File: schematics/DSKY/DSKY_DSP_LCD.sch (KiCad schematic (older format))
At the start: 12 parts

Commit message: Minor DSKY tweaks.
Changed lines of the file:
@@
 $Descr A 8500 11000 portrait
 encoding utf-8
-Sheet 12 15
+Sheet 11 15
 Title ""
 Date ""
@@
 	1450 8250 1250 8250
 Wire Bus Line
-	700  2550 7000 2550
-Wire Bus Line
 	700  4500 7200 4500
 Wire Bus Line
+	700  2550 7200 2550
+Wire Bus Line
 	700  6500 7200 6500

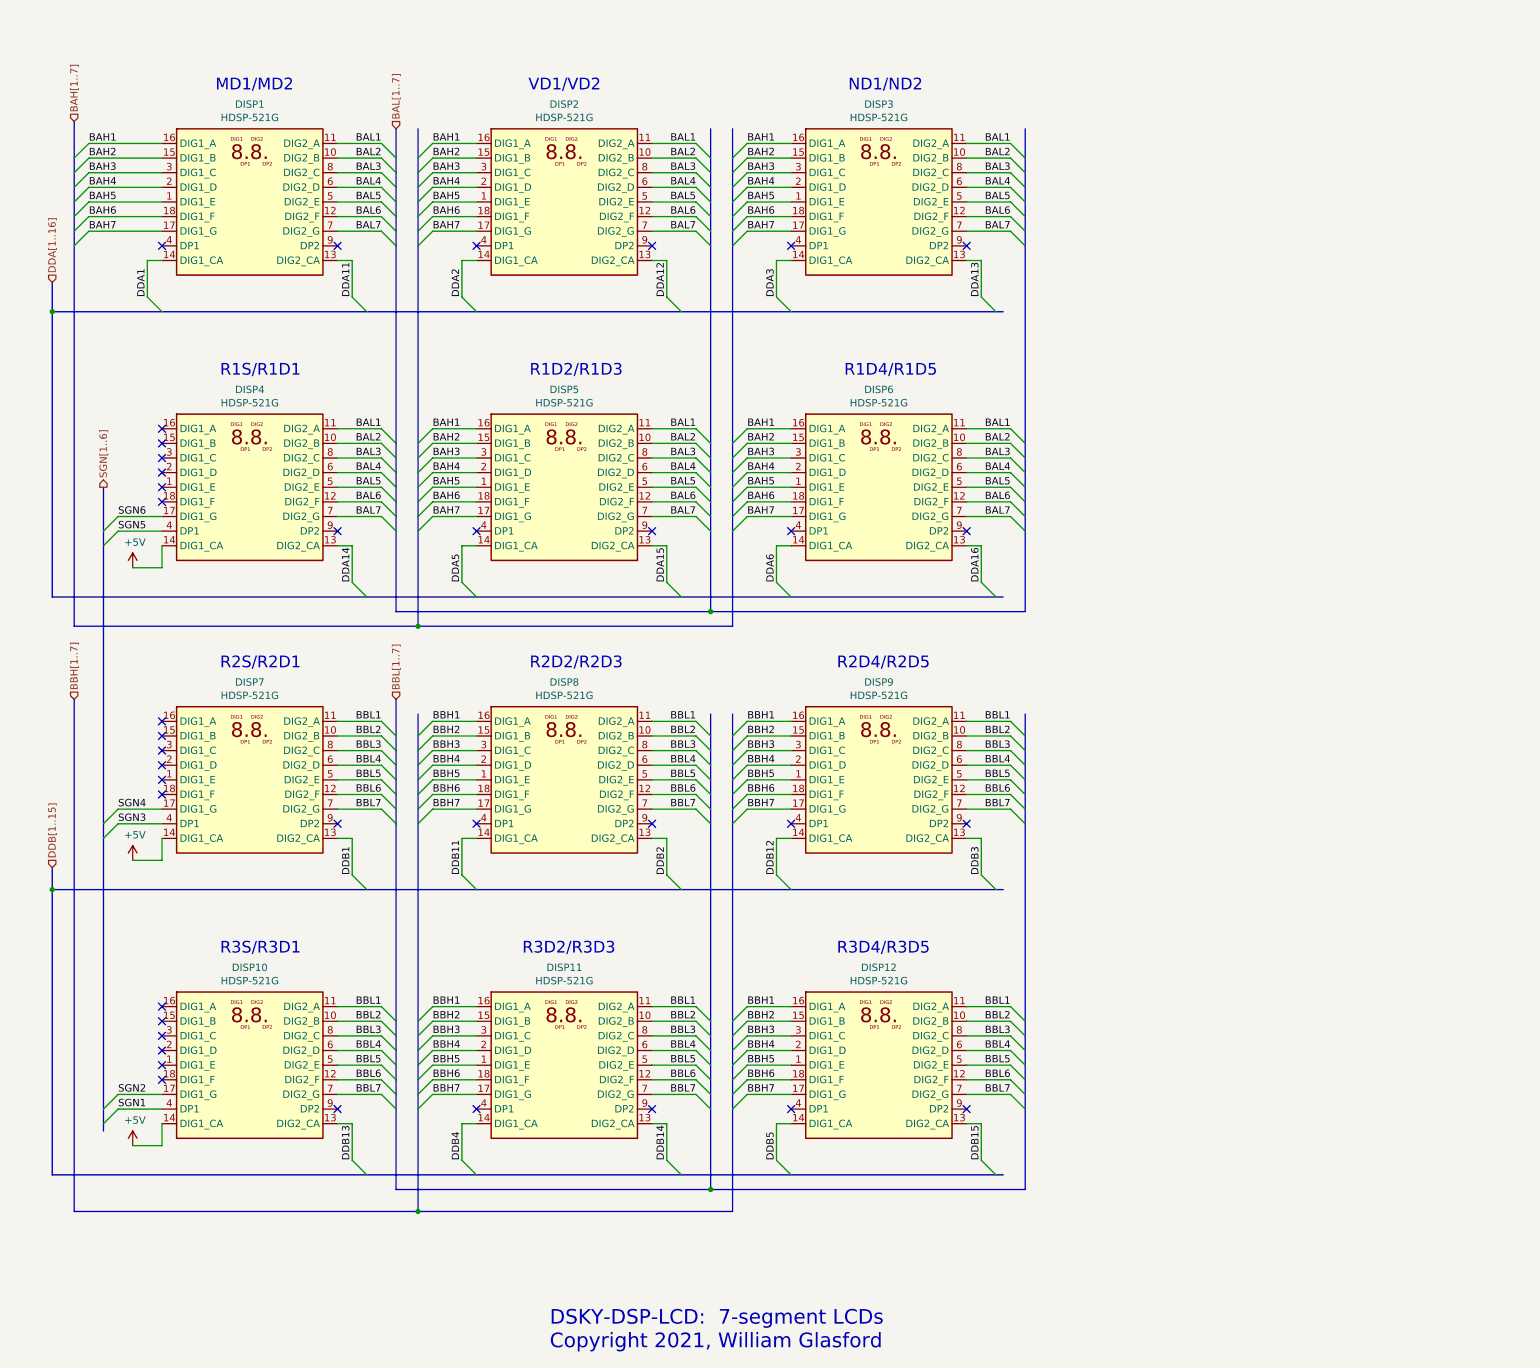
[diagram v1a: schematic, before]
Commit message: Using 4 LED driver chips.
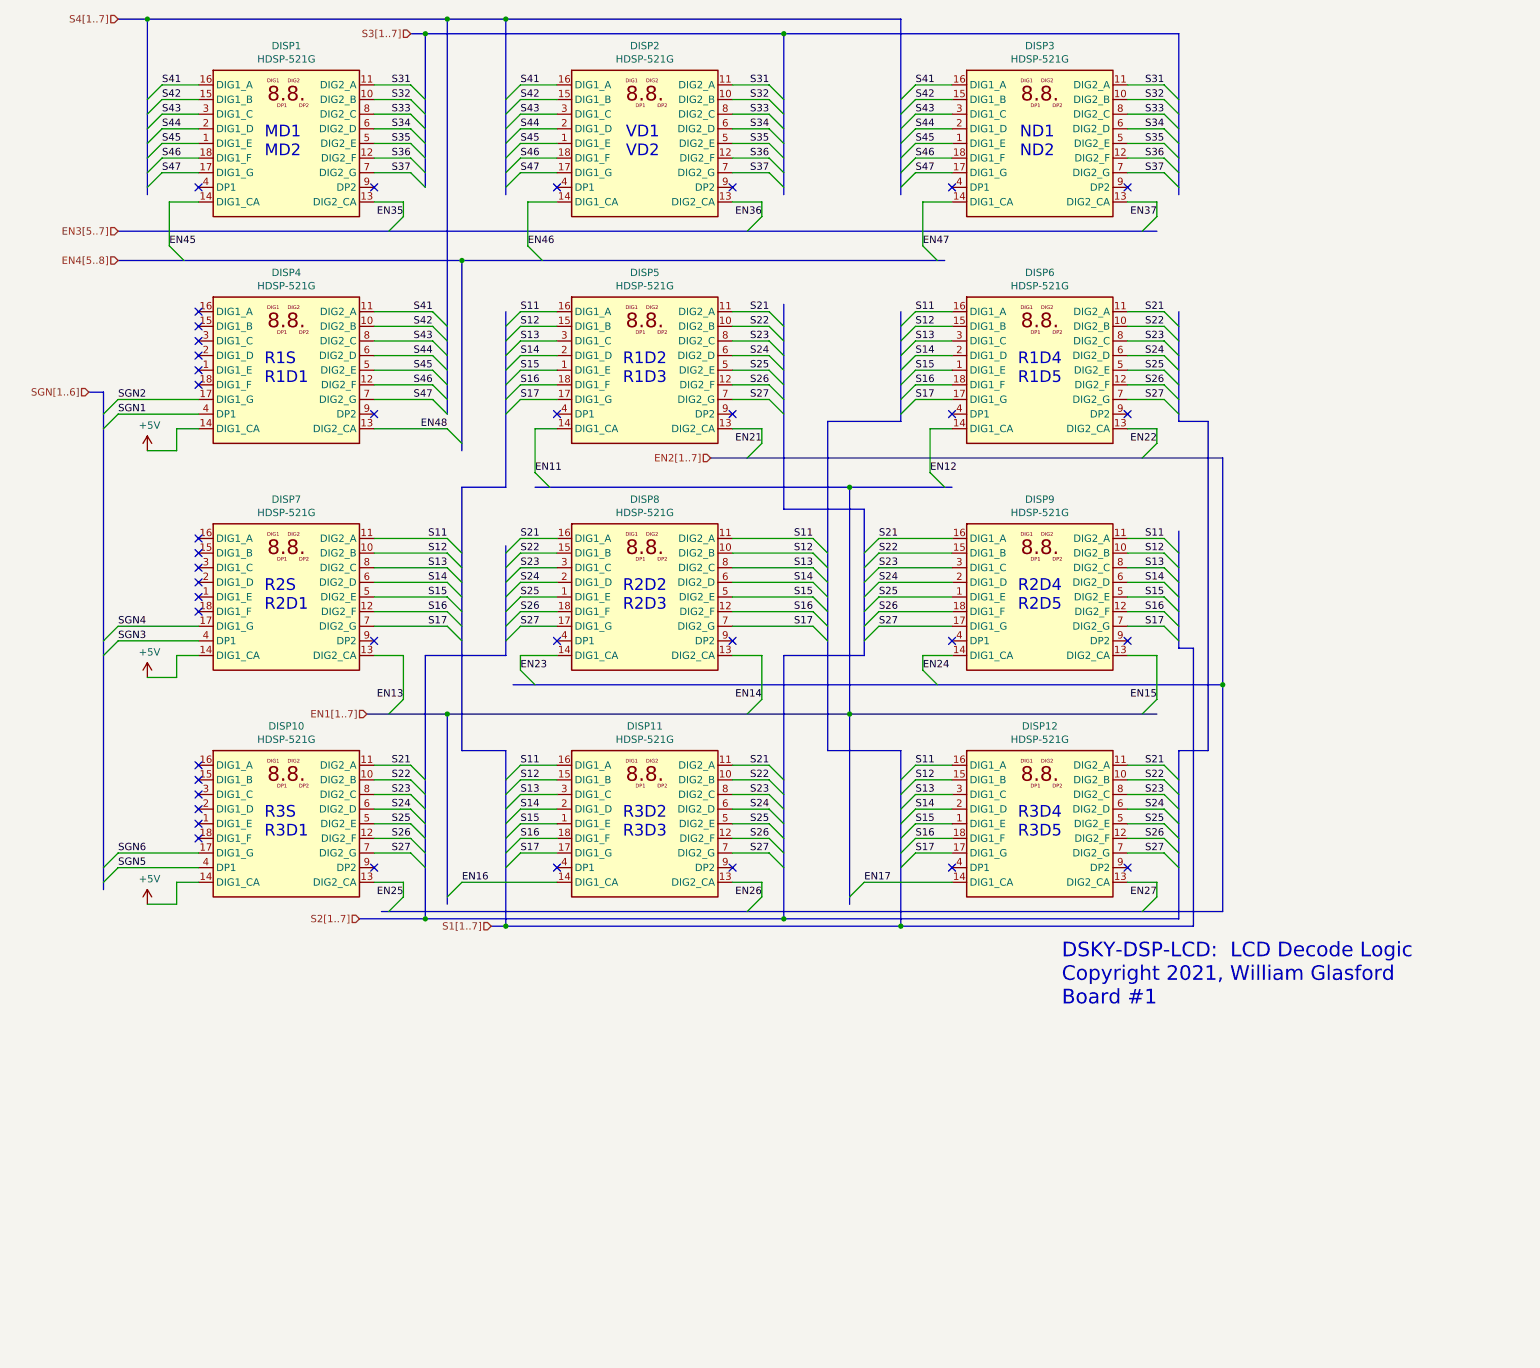
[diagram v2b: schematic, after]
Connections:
- net SGN1: now also DISP4.4 (DP1); no longer DISP10.4 (DP1)
- net SGN2: now also DISP4.17 (DIG1_G); no longer DISP10.17 (DIG1_G)
- net SGN5: now also DISP10.4 (DP1); no longer DISP4.4 (DP1)
- net SGN6: now also DISP10.17 (DIG1_G); no longer DISP4.17 (DIG1_G)
- net BAH1 renamed S41
- net S41: now also DISP4.11 (DIG2_A); no longer DISP5.16 (DIG1_A), DISP6.16 (DIG1_A)
- net BAH2 renamed S42
- net S42: now also DISP4.10 (DIG2_B); no longer DISP5.15 (DIG1_B), DISP6.15 (DIG1_B)
- net BAH3 renamed S43
- net S43: now also DISP4.8 (DIG2_C); no longer DISP5.3 (DIG1_C), DISP6.3 (DIG1_C)
- net BAH4 renamed S44
- net S44: now also DISP4.6 (DIG2_D); no longer DISP5.2 (DIG1_D), DISP6.2 (DIG1_D)
- net BAH5 renamed S45
- net S45: now also DISP4.5 (DIG2_E); no longer DISP5.1 (DIG1_E), DISP6.1 (DIG1_E)
- net BAH6 renamed S46
- net S46: now also DISP4.12 (DIG2_F); no longer DISP5.18 (DIG1_F), DISP6.18 (DIG1_F)
- net BAH7 renamed S47
- net S47: now also DISP4.7 (DIG2_G); no longer DISP5.17 (DIG1_G), DISP6.17 (DIG1_G)
- net BAL1 renamed S31
- net S31: no longer DISP4.11 (DIG2_A), DISP5.11 (DIG2_A), DISP6.11 (DIG2_A)
- net BAL2 renamed S32
- net S32: no longer DISP4.10 (DIG2_B), DISP5.10 (DIG2_B), DISP6.10 (DIG2_B)
- net BAL3 renamed S33
- net S33: no longer DISP4.8 (DIG2_C), DISP5.8 (DIG2_C), DISP6.8 (DIG2_C)
- net BAL4 renamed S34
- net S34: no longer DISP4.6 (DIG2_D), DISP5.6 (DIG2_D), DISP6.6 (DIG2_D)
- net BAL5 renamed S35
- net S35: no longer DISP4.5 (DIG2_E), DISP5.5 (DIG2_E), DISP6.5 (DIG2_E)
- net BAL6 renamed S36
- net S36: no longer DISP4.12 (DIG2_F), DISP5.12 (DIG2_F), DISP6.12 (DIG2_F)
- net BAL7 renamed S37
- net S37: no longer DISP4.7 (DIG2_G), DISP5.7 (DIG2_G), DISP6.7 (DIG2_G)
- net BBH1 renamed S11
- net S11: now also DISP5.16 (DIG1_A), DISP6.16 (DIG1_A), DISP7.11 (DIG2_A), DISP8.11 (DIG2_A), DISP9.11 (DIG2_A); no longer DISP8.16 (DIG1_A), DISP9.16 (DIG1_A)
- net BBH2 renamed S12
- net S12: now also DISP5.15 (DIG1_B), DISP6.15 (DIG1_B), DISP7.10 (DIG2_B), DISP8.10 (DIG2_B), DISP9.10 (DIG2_B); no longer DISP8.15 (DIG1_B), DISP9.15 (DIG1_B)
- net BBH3 renamed S13
- net S13: now also DISP5.3 (DIG1_C), DISP6.3 (DIG1_C), DISP7.8 (DIG2_C), DISP8.8 (DIG2_C), DISP9.8 (DIG2_C); no longer DISP8.3 (DIG1_C), DISP9.3 (DIG1_C)
- net BBH4 renamed S14
- net S14: now also DISP5.2 (DIG1_D), DISP6.2 (DIG1_D), DISP7.6 (DIG2_D), DISP8.6 (DIG2_D), DISP9.6 (DIG2_D); no longer DISP8.2 (DIG1_D), DISP9.2 (DIG1_D)
- net BBH5 renamed S15
- net S15: now also DISP5.1 (DIG1_E), DISP6.1 (DIG1_E), DISP7.5 (DIG2_E), DISP8.5 (DIG2_E), DISP9.5 (DIG2_E); no longer DISP8.1 (DIG1_E), DISP9.1 (DIG1_E)
- net BBH6 renamed S16
- net S16: now also DISP5.18 (DIG1_F), DISP6.18 (DIG1_F), DISP7.12 (DIG2_F), DISP8.12 (DIG2_F), DISP9.12 (DIG2_F); no longer DISP8.18 (DIG1_F), DISP9.18 (DIG1_F)
- net BBH7 renamed S17
- net S17: now also DISP5.17 (DIG1_G), DISP6.17 (DIG1_G), DISP7.7 (DIG2_G), DISP8.7 (DIG2_G), DISP9.7 (DIG2_G); no longer DISP8.17 (DIG1_G), DISP9.17 (DIG1_G)
- net BBL1 renamed S21
- net S21: now also DISP5.11 (DIG2_A), DISP6.11 (DIG2_A), DISP8.16 (DIG1_A), DISP9.16 (DIG1_A); no longer DISP7.11 (DIG2_A), DISP8.11 (DIG2_A), DISP9.11 (DIG2_A)
- net BBL2 renamed S22
- net S22: now also DISP5.10 (DIG2_B), DISP6.10 (DIG2_B), DISP8.15 (DIG1_B), DISP9.15 (DIG1_B); no longer DISP7.10 (DIG2_B), DISP8.10 (DIG2_B), DISP9.10 (DIG2_B)
- net BBL3 renamed S23
- net S23: now also DISP5.8 (DIG2_C), DISP6.8 (DIG2_C), DISP8.3 (DIG1_C), DISP9.3 (DIG1_C); no longer DISP7.8 (DIG2_C), DISP8.8 (DIG2_C), DISP9.8 (DIG2_C)
- net BBL4 renamed S24
- net S24: now also DISP5.6 (DIG2_D), DISP6.6 (DIG2_D), DISP8.2 (DIG1_D), DISP9.2 (DIG1_D); no longer DISP7.6 (DIG2_D), DISP8.6 (DIG2_D), DISP9.6 (DIG2_D)
- net BBL5 renamed S25
- net S25: now also DISP5.5 (DIG2_E), DISP6.5 (DIG2_E), DISP8.1 (DIG1_E), DISP9.1 (DIG1_E); no longer DISP7.5 (DIG2_E), DISP8.5 (DIG2_E), DISP9.5 (DIG2_E)
- net BBL6 renamed S26
- net S26: now also DISP5.12 (DIG2_F), DISP6.12 (DIG2_F), DISP8.18 (DIG1_F), DISP9.18 (DIG1_F); no longer DISP7.12 (DIG2_F), DISP8.12 (DIG2_F), DISP9.12 (DIG2_F)
- net BBL7 renamed S27
- net S27: now also DISP5.7 (DIG2_G), DISP6.7 (DIG2_G), DISP8.17 (DIG1_G), DISP9.17 (DIG1_G); no longer DISP7.7 (DIG2_G), DISP8.7 (DIG2_G), DISP9.7 (DIG2_G)
- net DDA1 renamed EN45
- net DDA11 renamed EN35
- net DDA12 renamed EN36
- net DDA13 renamed EN37
- net DDA14 renamed EN48
- net DDA15 renamed EN21
- net DDA16 renamed EN22
- net DDA2 renamed EN46
- net DDA3 renamed EN47
- net DDA5 renamed EN11
- net DDA6 renamed EN12
- net DDB1 renamed EN13
- net DDB11 renamed EN23
- net DDB12 renamed EN24
- net DDB13 renamed EN25
- net DDB14 renamed EN26
- net DDB15 renamed EN27
- net DDB2 renamed EN14
- net DDB3 renamed EN15
- net DDB4 renamed EN16
- net DDB5 renamed EN17
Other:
- note added: "DSKY-DSP-LCD: LCD Decode Logic\nCopyright 2021, William Glasford\nBoard #1"
- note added: "MD1\nMD2"
- note added: "ND1\nND2"
- note added: "R1D2\nR1D3"
- note added: "R1D4\nR1D5"
- note added: "R1S\nR1D1"
- note added: "R2D2\nR2D3"
- note added: "R2D4\nR2D5"
- note added: "R2S\nR2D1"
- note added: "R3D2\nR3D3"
- note added: "R3D4\nR3D5"
- note added: "R3S\nR3D1"
- note added: "VD1\nVD2"
- note removed: "DSKY-DSP-LCD: 7-segment LCDs\nCopyright 2021, William Glasford"
- note removed: "MD1/MD2"
- note removed: "ND1/ND2"
- note removed: "R1D2/R1D3"
- note removed: "R1D4/R1D5"
- note removed: "R1S/R1D1"
- note removed: "R2D2/R2D3"
- note removed: "R2D4/R2D5"
- note removed: "R2S/R2D1"
- note removed: "R3D2/R3D3"
- note removed: "R3D4/R3D5"
- note removed: "R3S/R3D1"
- note removed: "VD1/VD2"
- moved on the sheet: DISP1, DISP10, DISP11, DISP12, DISP2, DISP3, DISP4, DISP5, DISP6, DISP7, DISP8, DISP9
